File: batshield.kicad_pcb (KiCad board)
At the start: 2 copper layers, 67 parts, among them J1 I/O 1, J2 mic in 1/4'', J3 arduinoUnoPinout, J4 I/O 2, J5 mic in 1/4'', J6 MIDI out, J7 MIDI IN, Q1 2N3904, SW1 RESET, SW10 SWT3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

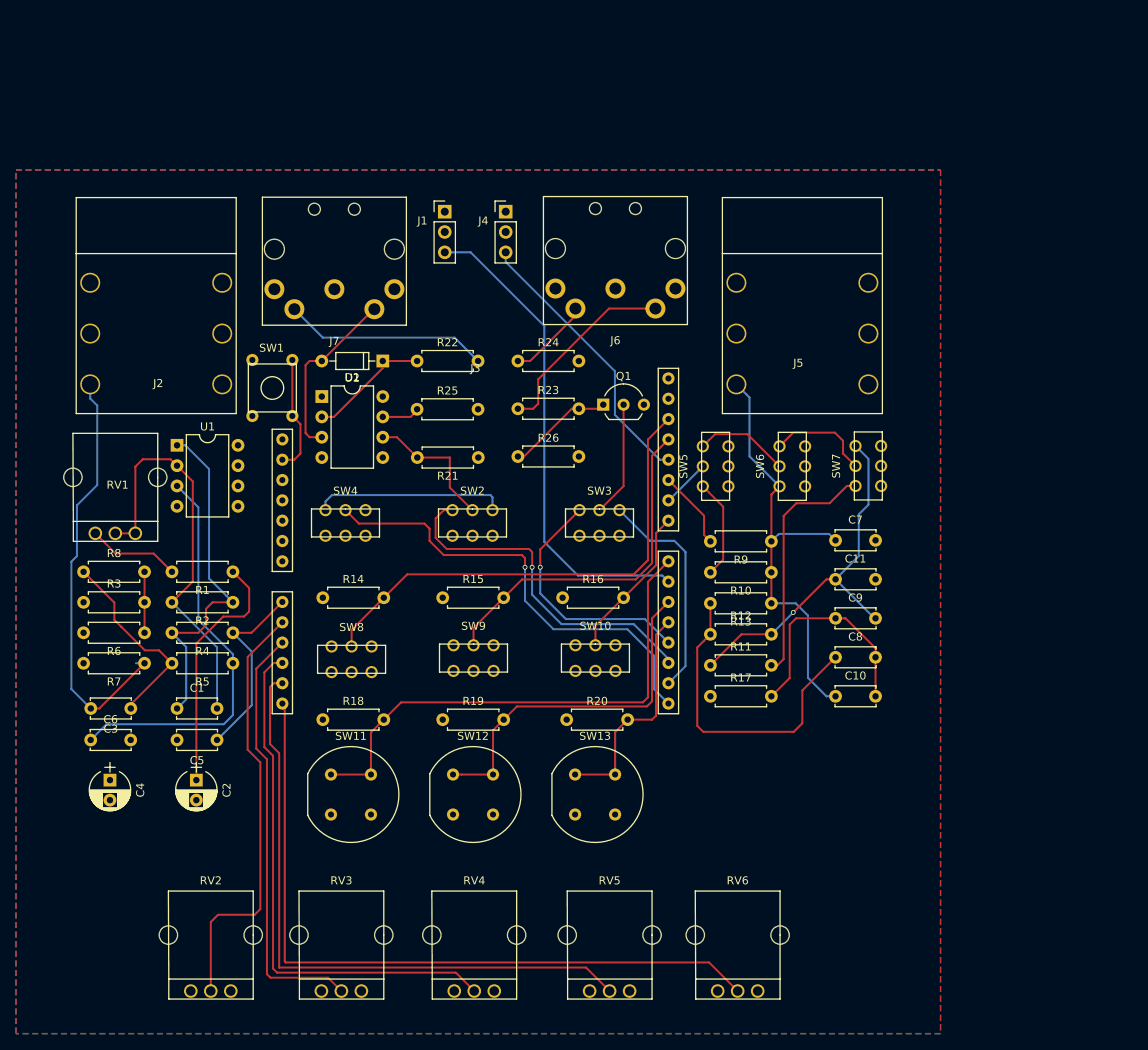
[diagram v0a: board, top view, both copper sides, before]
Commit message: añado algunos modelos 3d
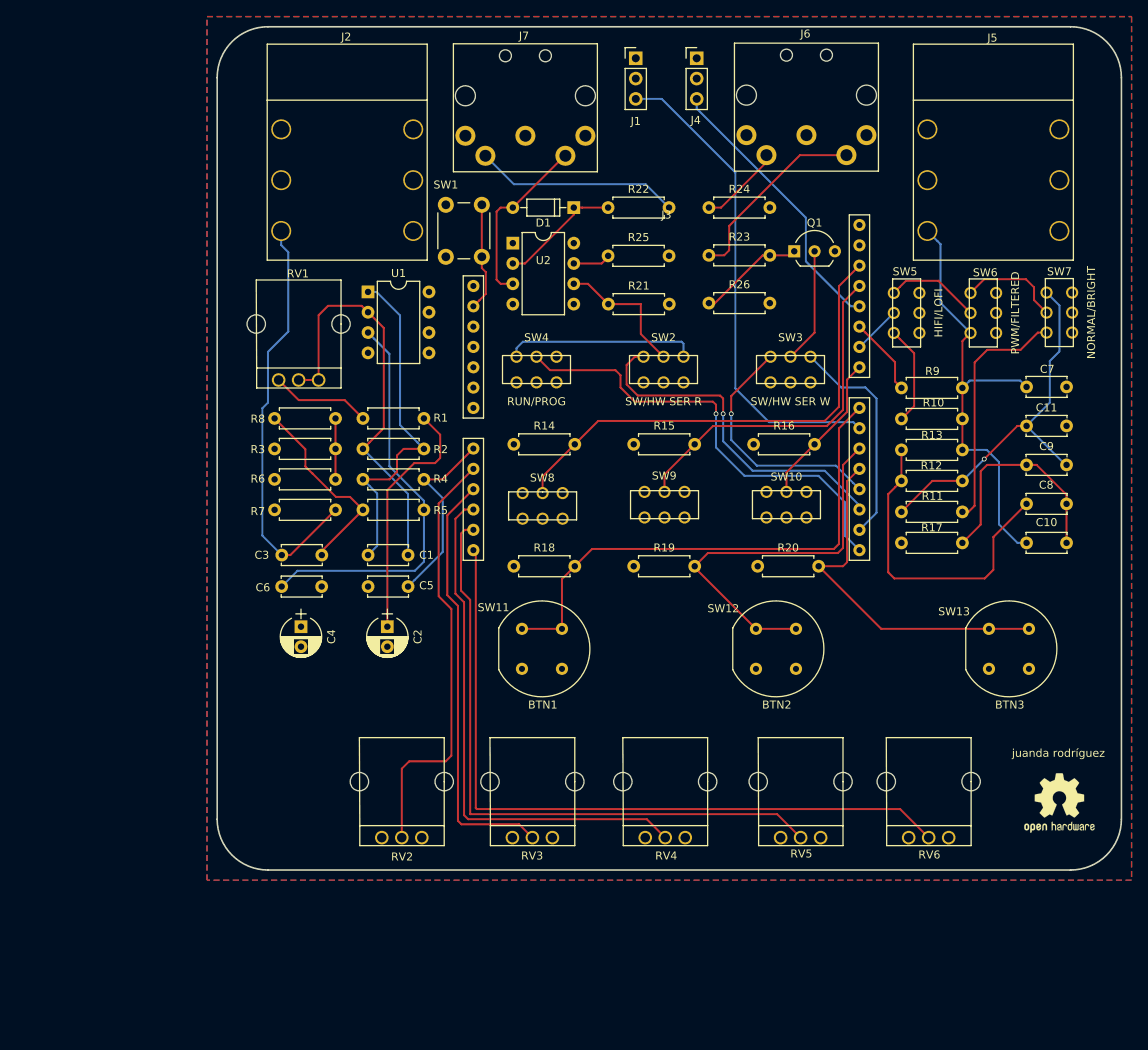
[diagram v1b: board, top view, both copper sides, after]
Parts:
- added REF***: OSHW-Logo2_9.8x8mm_SilkScreen, Symbols:OSHW-Logo2_9.8x8mm_SilkScreen, F.Cu at (195.2, 136.3)
- SW1: footprint conectores:pulsador_spst_mini -> Buttons_Switches_THT:SW_PUSH_6mm_h5mm
- moved SW13 54.8 mm to (188.9, 117.0)
- moved SW12 42.0 mm to (159.8, 117.0)
- moved SW9 30.6 mm to (145.8, 99.0)
- moved J4 30.6 mm to (149.9, 43.2)
- moved C10 30.6 mm to (191.1, 103.8)
- moved C7 30.6 mm to (191.1, 84.3)
- moved C8 30.6 mm to (191.1, 98.9)
- moved J1 30.6 mm to (142.2, 43.2)
- moved R11 30.6 mm to (175.5, 99.9)
- moved R13 30.6 mm to (183.1, 92.1)
- moved R14 30.6 mm to (127.0, 91.4)
- moved R16 30.6 mm to (157.0, 91.4)
- moved R17 30.6 mm to (175.5, 103.8)
- moved R22 30.6 mm to (138.8, 61.8)
- moved R6 30.6 mm to (104.7, 95.8)
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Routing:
- net BTN3: track 28.6 -> 45.6 mm
- net BTN2: track 45.2 -> 48.8 mm
- net Net-(J3-Pad2): track 14.7 -> 13.5 mm
- net Net-(C3-Pad2): track 53.3 -> 52.3 mm
- net BTN1: track 64.8 -> 65.7 mm
- net Net-(R1-Pad2): track 11.6 -> 12.5 mm
- net Net-(C1-Pad2): track 51.3 -> 52.2 mm
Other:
- board outline added: 113 x 105.4 mm
- board text added: "juanda rodríguez"

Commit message: quito transistor del circuito midi out
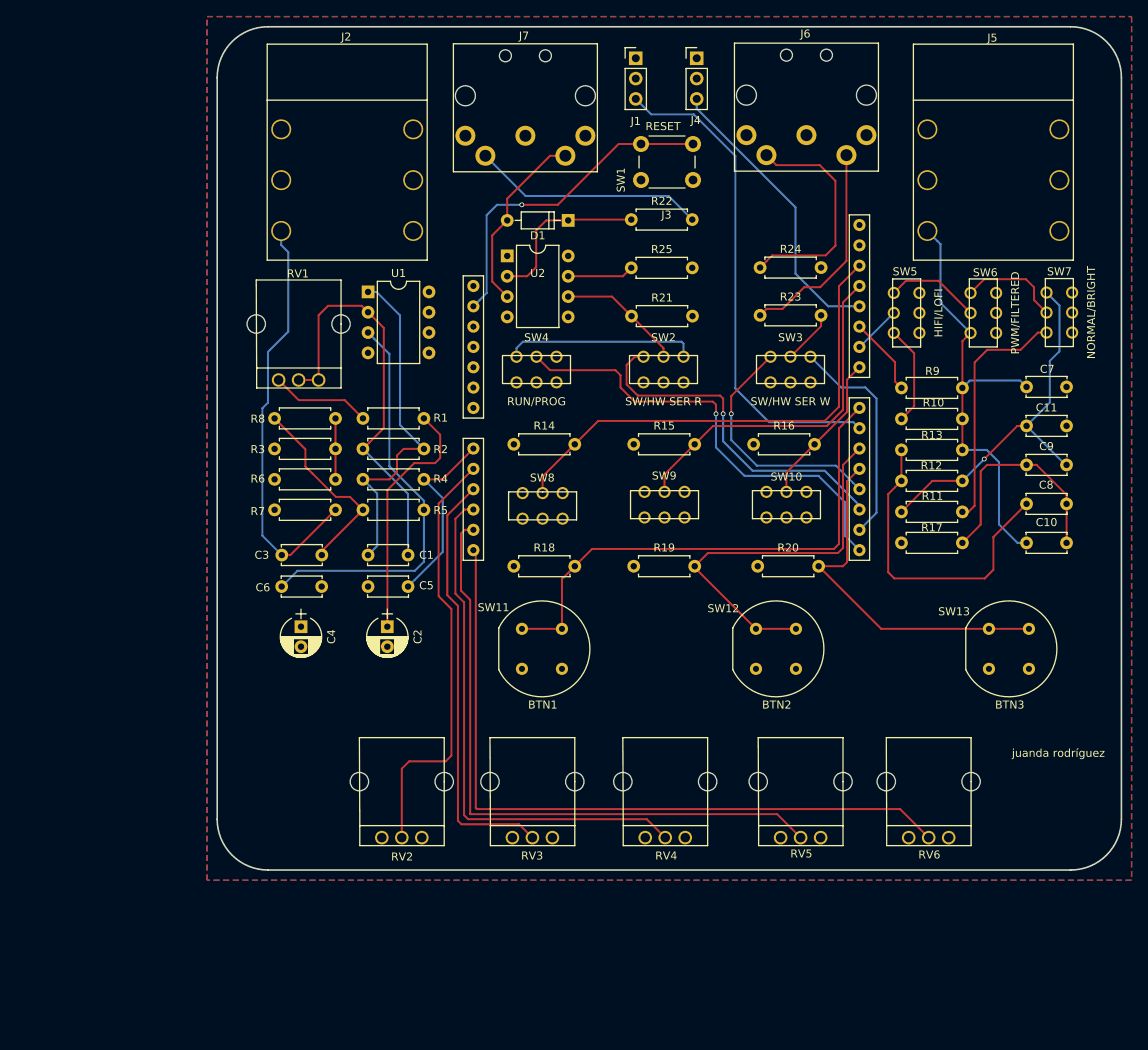
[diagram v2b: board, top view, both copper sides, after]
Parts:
- removed Q1: 2N3904, TO_SOT_Packages_THT:TO-92_Inline_Wide
- removed R26: 500, Resistors_THT:R_Axial_DIN0207_L6.3mm_D2.5mm_P7.62mm_Horizontal
- removed REF***: OSHW-Logo2_9.8x8mm_SilkScreen, Symbols:OSHW-Logo2_9.8x8mm_SilkScreen
- moved SW1 32.4 mm to (149.4, 58.4), turned to 180 degrees
- moved R24 9.86 mm to (157.8, 69.3)
- moved R23 9.86 mm to (157.8, 75.3)
- moved R22 3.26 mm to (141.7, 63.3)
- moved R25 3.26 mm to (141.7, 69.4)
- moved R21 3.26 mm to (149.3, 75.4)
- moved U2 1.75 mm to (126.2, 67.9)
- moved D1 1.75 mm to (133.8, 63.4)
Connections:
- R23 pad 2: Net-(Q1-Pad1) -> PORT-TX
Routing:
- net Net-(J3-Pad2): track 13.5 -> 41.6 mm, vias 0 -> 1
- net Net-(J6-Pad4): track 10.4 -> 29.5 mm
- net Net-(Q1-Pad1): track 13.4 -> 0.00 mm
- net PORT-TX: track 14.4 -> 6.76 mm
- net Net-(D1-Pad1): track 15.3 -> 21.1 mm
- net Net-(J6-Pad5): track 24.2 -> 27.8 mm
- net Net-(J7-Pad4): track 25.6 -> 29.2 mm
- net Net-(R25-Pad1): track 4.84 -> 8.32 mm
- net IO2: track 35.0 -> 36.6 mm
- net PORT-RX: track 17.2 -> 15.7 mm
- net IO1: track 60.8 -> 62.0 mm
- net Net-(D1-Pad2): track 22.2 -> 23.3 mm

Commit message: reduciendo el tamaño de la placa unos milimetros cuadrados
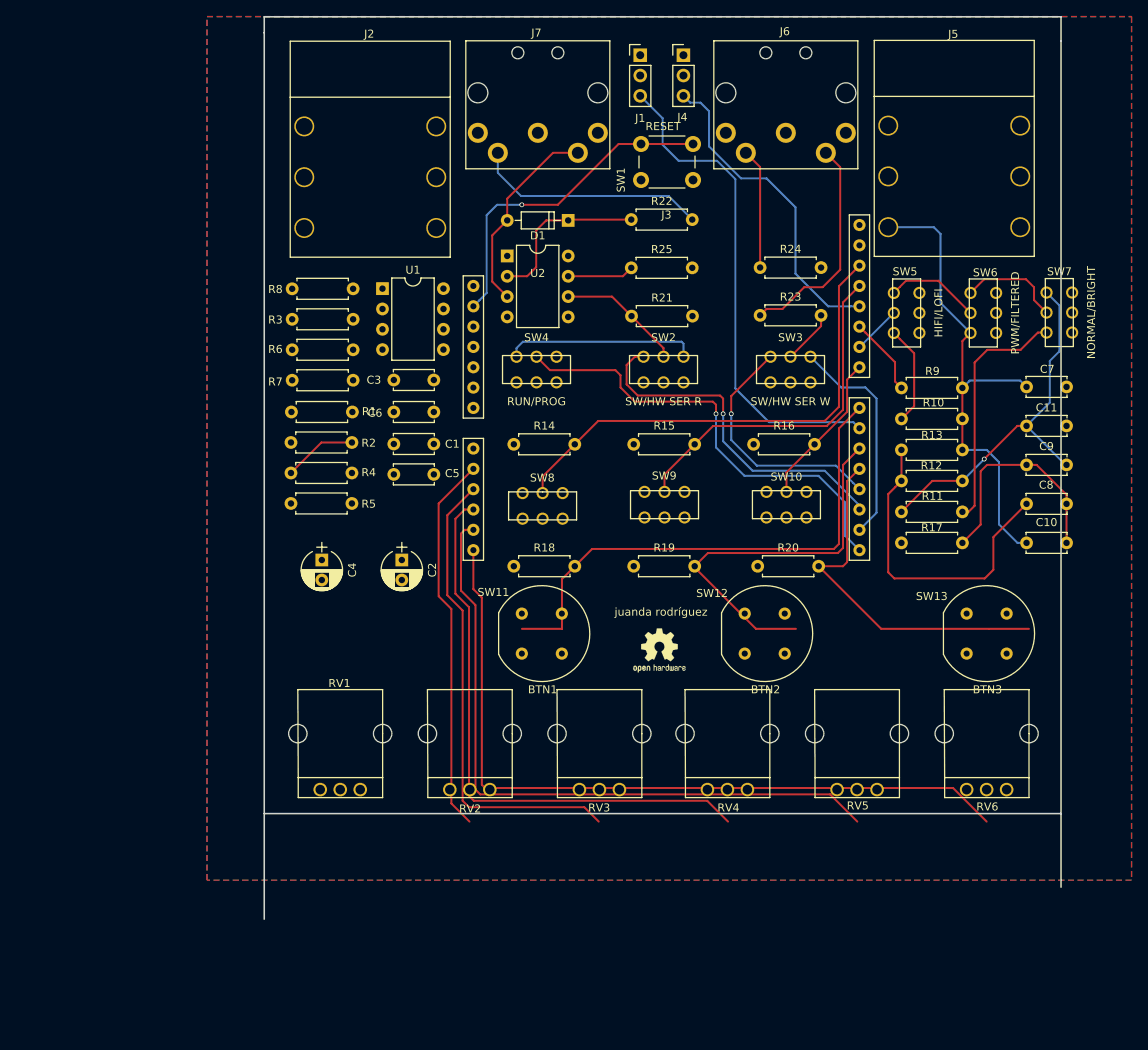
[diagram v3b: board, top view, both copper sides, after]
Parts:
- added REF***: OSHW-Logo2_7.3x6mm_SilkScreen, Symbols:OSHW-Logo2_7.3x6mm_SilkScreen, F.Cu at (145.2, 117.2)
- moved RV1 51.5 mm to (105.3, 134.6)
- moved C3 26.0 mm to (117.0, 83.4)
- moved C6 25.9 mm to (112.0, 87.4)
- moved R3 16.3 mm to (99.3, 75.8)
- moved R6 16.3 mm to (106.9, 79.6)
- moved R7 16.3 mm to (106.9, 83.4)
- moved R8 16.3 mm to (99.3, 72.0)
- moved C5 14.4 mm to (117.0, 95.2)
- moved C1 14.3 mm to (112.0, 91.4)
- moved RV2 10.4 mm to (121.5, 134.6)
- moved RV3 10.3 mm to (137.7, 134.6)
- moved RV4 9.82 mm to (153.7, 134.6)
- moved RV6 9.41 mm to (186.1, 134.6)
- moved RV5 9.26 mm to (169.9, 134.6)
- moved R2 9.04 mm to (106.8, 91.2)
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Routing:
- net Net-(C3-Pad2): track 52.3 -> 0.00 mm
- net Net-(C1-Pad2): track 52.2 -> 0.00 mm
- net Net-(C6-Pad1): track 50.6 -> 0.00 mm
- net Net-(C1-Pad1): track 44.2 -> 9.20 mm
- net Net-(C2-Pad1): track 31.1 -> 0.00 mm
- net Net-(C3-Pad1): track 24.8 -> 0.00 mm
- net IN: track 23.9 -> 0.00 mm
- net Net-(J6-Pad4): track 29.5 -> 15.1 mm
- net Net-(R1-Pad2): track 12.5 -> 0.00 mm
- net 2.5V: track 7.62 -> 0.00 mm
- net KNOB1: track 53.9 -> 47.6 mm
- net Net-(C10-Pad1): track 56.1 -> 62.0 mm
- net KNOB2: track 53.5 -> 59.2 mm
- net KNOB3: track 66.5 -> 71.8 mm
- net KNOB5: track 90.6 -> 95.3 mm
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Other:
- board size 113 x 105.4 mm -> 99.6 x 112.8 mm

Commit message: reduciendo el tamaño de la placa unos milimetros cuadrados ...
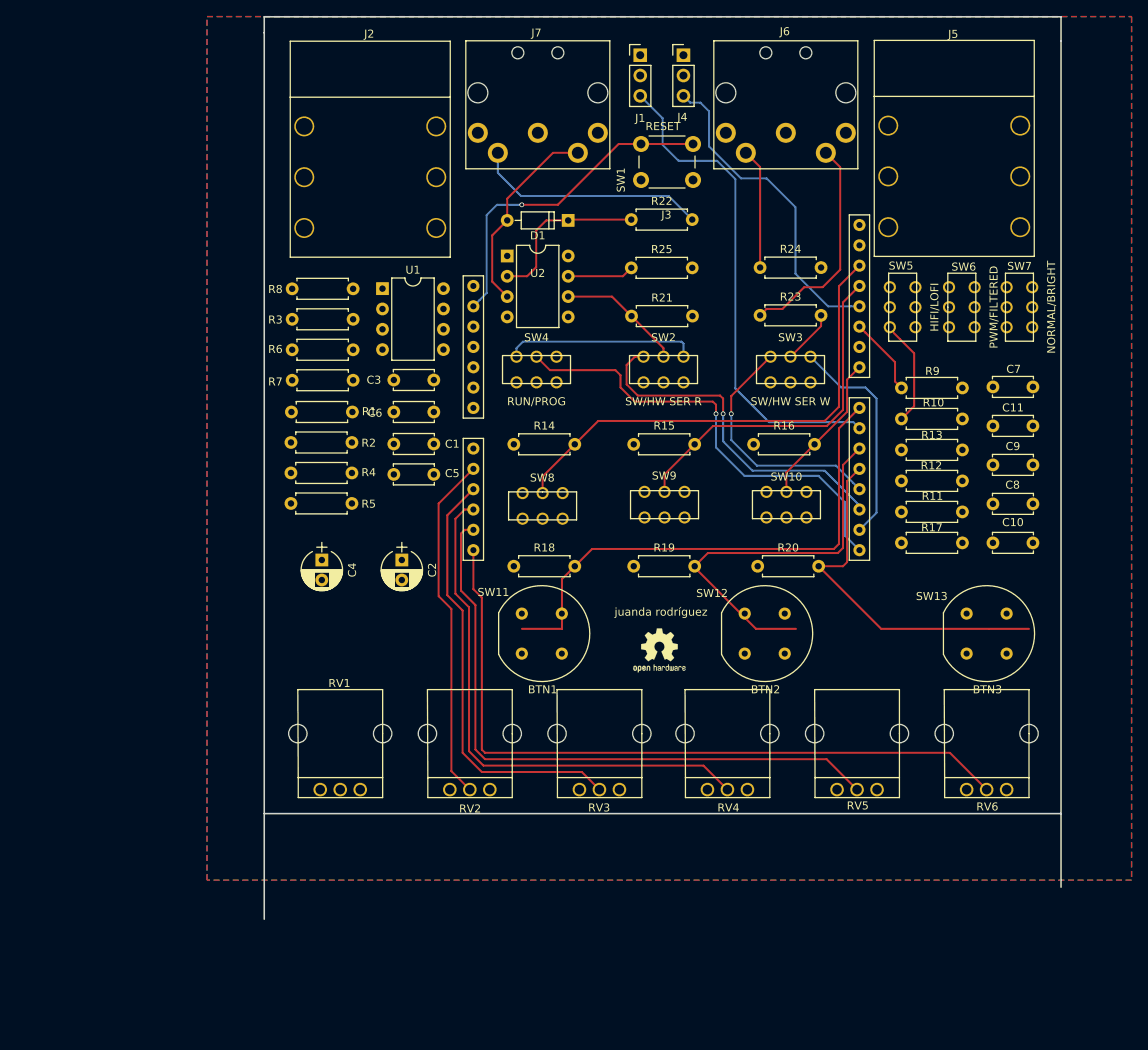
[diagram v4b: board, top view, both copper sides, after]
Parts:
- moved SW7 5.03 mm to (190.2, 74.3)
- moved C10 4.20 mm to (186.9, 103.8)
- moved C11 4.20 mm to (186.9, 89.1)
- moved C7 4.20 mm to (186.9, 84.3)
- moved C8 4.20 mm to (186.9, 98.9)
- moved C9 4.20 mm to (186.9, 94.0)
- moved SW6 2.78 mm to (183.0, 74.3)
- moved SW5 0.87 mm to (175.6, 74.3)
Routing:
- net Net-(C10-Pad1): track 62.0 -> 0.00 mm
- net Net-(C11-Pad1): track 46.1 -> 0.00 mm, vias 1 -> 0
- net Net-(C8-Pad1): track 39.9 -> 0.00 mm
- net Net-(R11-Pad2): track 30.3 -> 0.00 mm
- net Net-(C10-Pad2): track 28.5 -> 0.00 mm
- net Net-(SW6-Pad3): track 12.9 -> 0.00 mm
- net Net-(SW5-Pad3): track 11.9 -> 0.00 mm
- net Net-(C1-Pad1): track 9.20 -> 0.00 mm
- net PWM1: track 6.06 -> 0.04 mm
- net KNOB2: track 59.2 -> 54.1 mm
- net KNOB3: track 71.8 -> 66.8 mm
- net KNOB4: track 83.9 -> 79.3 mm
- net KNOB5: track 95.3 -> 91.0 mm
- net KNOB1: track 47.6 -> 43.6 mm

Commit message: reducido a un tamaño aprox de 100mm x 100mm
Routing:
- net Net-(C1-Pad2): track 0.00 -> 100.2 mm, vias 0 -> 1
- net Net-(C3-Pad1): track 0.00 -> 66.9 mm
- net Net-(C10-Pad2): track 0.00 -> 56.1 mm
- net Net-(R1-Pad2): track 0.00 -> 53.5 mm, vias 0 -> 1
- net Net-(C1-Pad1): track 0.00 -> 52.5 mm
- net Net-(C10-Pad1): track 0.00 -> 50.2 mm
- net Net-(C11-Pad1): track 0.00 -> 43.4 mm
- net Net-(C8-Pad1): track 0.00 -> 33.7 mm
- net Net-(R11-Pad2): track 0.00 -> 33.6 mm, vias 0 -> 1
- net IN: track 0.00 -> 28.7 mm, vias 0 -> 2
- net Net-(C3-Pad2): track 0.00 -> 26.7 mm
- net Net-(C6-Pad1): track 0.00 -> 26.5 mm
- net Net-(C2-Pad1): track 0.00 -> 22.2 mm
- net Net-(SW5-Pad3): track 0.00 -> 11.4 mm
- net Net-(SW6-Pad3): track 0.00 -> 11.3 mm
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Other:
- board size 99.6 x 112.8 mm -> 99.6 x 99.6 mm

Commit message: reducidooooo
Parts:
- J2 (AUDIO IN): renamed from J2
- J5 (AUDIO OUT): renamed from J5
- J6 (MIDI OUT): renamed from J6
- J7 (MIDI IN): renamed from J7
- moved C5 14.1 mm to (116.4, 109.3)
- moved R5 10.5 mm to (107.8, 109.3)
- moved R4 9.02 mm to (107.7, 104.0)
- moved C1 9.01 mm to (111.4, 100.4)
- moved C2 8.82 mm to (114.0, 114.7)
- moved C4 8.77 mm to (103.4, 114.7)
- moved R2 7.52 mm to (107.8, 98.7)
- moved R1 6.05 mm to (107.7, 93.4)
- moved C6 5.50 mm to (111.4, 92.9)
- moved R7 4.67 mm to (107.8, 88.0)
- moved R6 3.20 mm to (107.8, 82.7)
- moved C3 2.86 mm to (116.4, 86.2)
- moved R3 1.80 mm to (100.2, 77.4)
- moved R8 0.91 mm to (100.2, 72.1)
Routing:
- net GND: track 0.00 -> 16.1 mm
- net Net-(C1-Pad1): track 52.5 -> 66.8 mm
- net Net-(C6-Pad1): track 26.5 -> 36.4 mm, vias 0 -> 2
- net Net-(C3-Pad2): track 26.7 -> 34.5 mm
- net Net-(R1-Pad2): track 53.5 -> 48.5 mm, vias 1 -> 0
- net Net-(C1-Pad2): track 100.2 -> 96.7 mm, vias 1 -> 2
- net 2.5V: track 7.62 -> 10.6 mm
- net Net-(C2-Pad1): track 22.2 -> 25.0 mm, vias 0 -> 2
- net IN: track 28.7 -> 27.5 mm, vias 2 -> 0
- net Net-(C3-Pad1): track 66.9 -> 66.0 mm, vias 0 -> 1
